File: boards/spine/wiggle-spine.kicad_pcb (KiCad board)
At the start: 2 copper layers, 173 parts, among them CON1 5-24V 5A, CON2 5-24V 16A, CON3 PLR135, CON4 PLT133, CON5 USB-B, CON6 XLR-3 Female, CON7 USB-A, Q1 IRFML8244, Q2 IRFML8244, Q3 IRFML8244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

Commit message: Component clustering around top and bottom I/O ports
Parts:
- added REF**: 1pin, Connect:1pin, F.Cu at (53.3, 170.2)
- added REF**: 1pin, Connect:1pin, F.Cu at (111.8, 170.2)
- added REF**: 1pin, Connect:1pin, F.Cu at (111.8, 45.7)
- added REF**: 1pin, Connect:1pin, F.Cu at (53.3, 45.7)
- moved C74 224.8 mm to (-57.9, 255.4), turned to 270 degrees
- moved C76 220.3 mm to (-54.9, 260.1)
- moved C77 220.2 mm to (-61.0, 260.1)
- moved U13 219.6 mm to (-55.1, 254.9), turned to 0 degrees
- moved U14 218.5 mm to (-57.9, 259.2)
- moved C75 217.7 mm to (-52.3, 256.0), turned to 270 degrees
- moved C32 209.8 mm to (-28.4, 273.9)
- moved C35 209.8 mm to (-34.6, 290.4)
- moved C36 209.8 mm to (-57.7, 266.3)
- moved C41 209.8 mm to (-28.4, 279.0)
- moved R16 209.8 mm to (-22.1, 267.0)
- moved R17 209.8 mm to (-24.6, 267.0)
- moved R18 209.8 mm to (-17.0, 267.0)
- moved R19 209.8 mm to (-19.6, 267.0)
- moved U7 209.8 mm to (-43.4, 274.1)
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
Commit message: Try 2.7" width
Probably too narrow to fit the DCDCs, but it looks nice doesn't it.
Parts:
- moved R15 232.0 mm to (102.5, 106.2), turned to 270 degrees
- moved C35 228.5 mm to (99.9, 105.7), turned to 270 degrees
- moved C39 225.1 mm to (98.0, 109.7), turned to 180 degrees
- moved C34 224.9 mm to (97.4, 106.2), turned to 90 degrees
- moved C38 224.6 mm to (98.0, 112.3), turned to 180 degrees
- moved C31 223.8 mm to (98.0, 118.0), turned to 180 degrees
- moved C33 223.5 mm to (98.0, 120.5), turned to 180 degrees
- moved C41 214.2 mm to (88.5, 99.6), turned to 270 degrees
- moved C40 210.7 mm to (86.0, 99.6), turned to 270 degrees
- moved C32 207.2 mm to (83.4, 99.6), turned to 270 degrees
- moved C44 206.9 mm to (86.6, 128.8), turned to 90 degrees
- moved U7 203.9 mm to (83.6, 114.6), turned to 180 degrees
- moved C46 203.7 mm to (80.9, 99.6), turned to 270 degrees
- moved R18 201.8 mm to (76.5, 88.1), turned to 180 degrees
- moved R19 200.7 mm to (76.5, 90.7), turned to 180 degrees
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
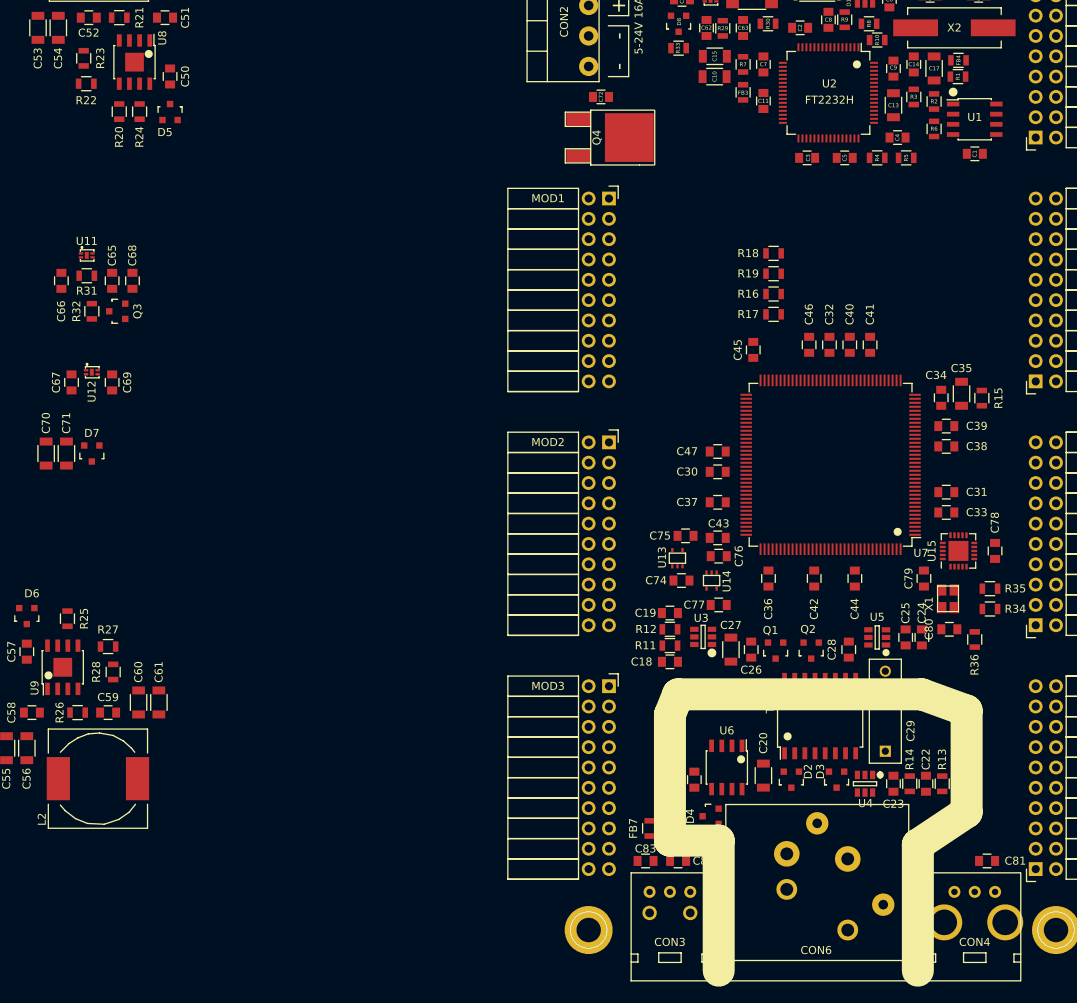
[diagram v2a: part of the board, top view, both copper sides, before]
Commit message: More component packing
If this routing is at all realistic, maybe 2.7" works after all. Haven't placed the DCDCs yet, but I think they'll fit.
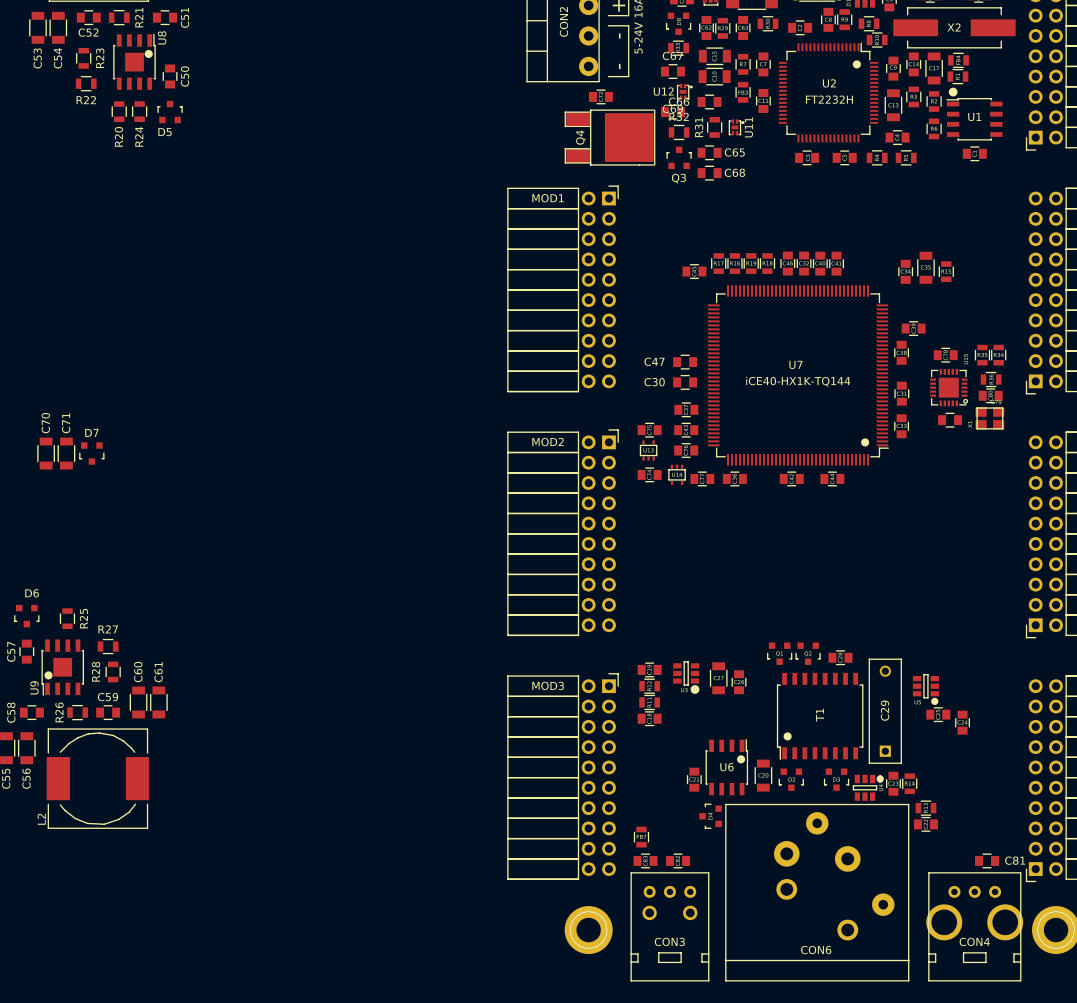
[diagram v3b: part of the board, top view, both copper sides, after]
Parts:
- moved C67 84.6 mm to (63.9, 65.4), turned to 180 degrees
- moved C66 84.1 mm to (68.5, 69.2), turned to 180 degrees
- moved U11 82.6 mm to (71.6, 72.4), turned to 180 degrees
- moved U12 81.8 mm to (65.2, 67.9), turned to 180 degrees
- moved R31 80.6 mm to (69.1, 72.4), turned to 270 degrees
- moved C69 77.8 mm to (63.9, 70.5), turned to 0 degrees
- moved R32 76.7 mm to (64.6, 73.0), turned to 180 degrees
- moved C65 76.4 mm to (68.5, 75.6), turned to 0 degrees
- moved C68 73.4 mm to (68.5, 78.1), turned to 0 degrees
- moved Q3 72.8 mm to (64.6, 76.2), turned to 0 degrees
- moved R36 32.6 mm to (103.6, 103.9), turned to 180 degrees
- moved R34 31.7 mm to (104.6, 100.9), turned to 270 degrees
- moved C80 29.6 mm to (103.6, 105.9), turned to 0 degrees
- moved R35 29.2 mm to (102.6, 100.9), turned to 270 degrees
- moved C78 25.2 mm to (98.0, 100.9), turned to 180 degrees
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
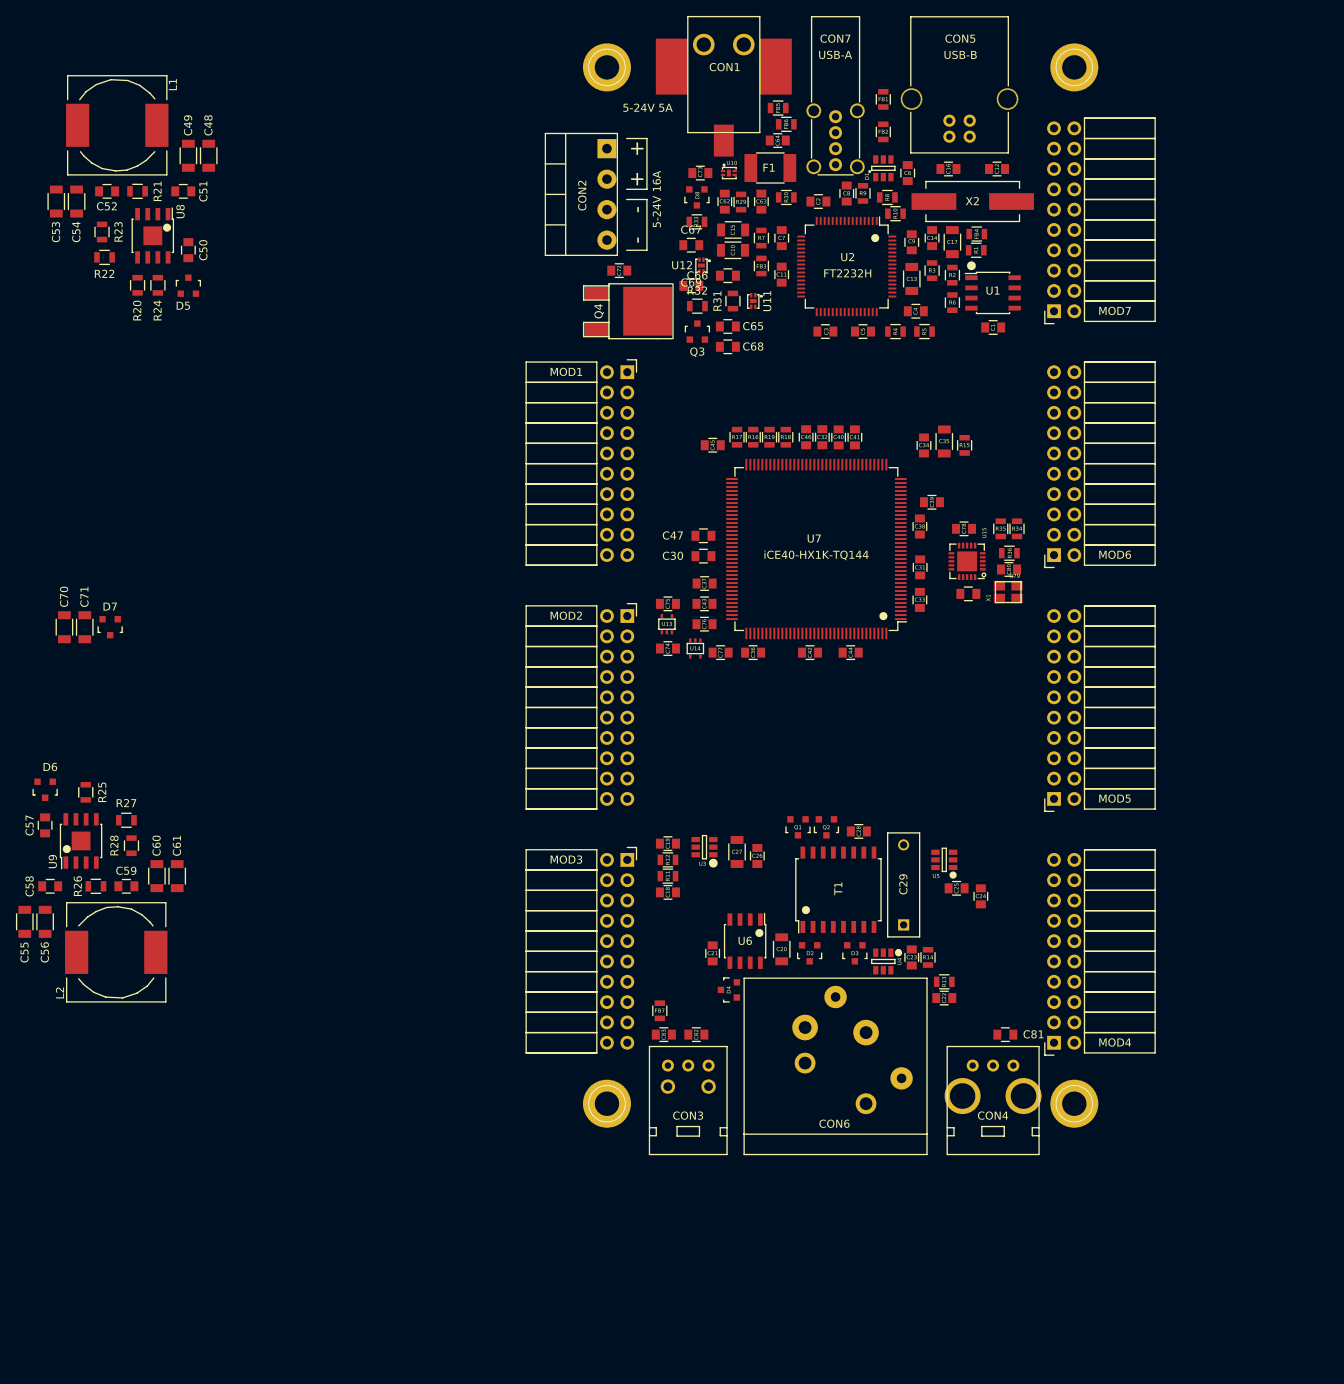
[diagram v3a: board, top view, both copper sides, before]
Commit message: Fix MOD pinouts, and layout for 2.7x5.2in
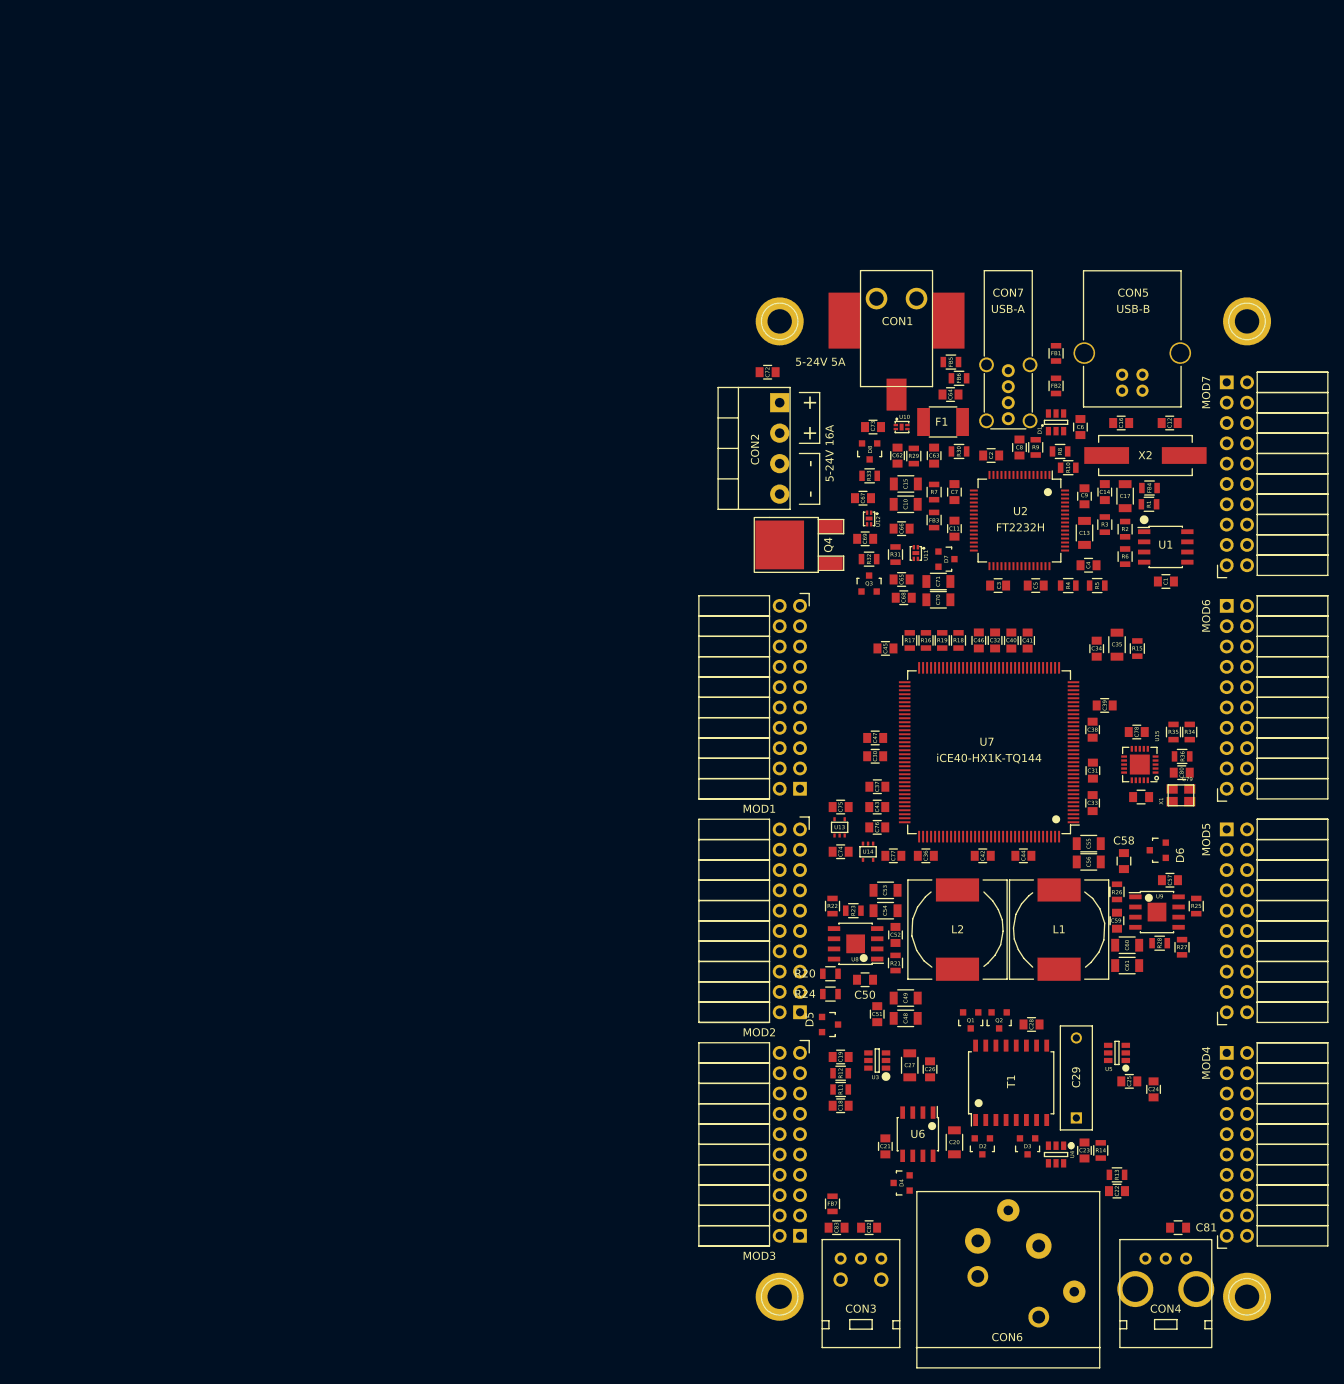
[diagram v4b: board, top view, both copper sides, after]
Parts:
- MOD1, MOD2, MOD3, MOD4, MOD5, MOD6, MOD7: footprint Socket_Strips:Socket_Strip_Angled_2x10 -> Socket_Strips:Socket_Strip_Angled_2x10_Mirror
- moved L1 154.8 mm to (109.9, 151.0), turned to 90 degrees
- moved C57 140.8 mm to (123.7, 144.8), turned to 180 degrees
- moved R25 139.5 mm to (127.0, 148.0)
- moved D6 139.3 mm to (122.2, 141.0), turned to 90 degrees
- moved C48 138.6 mm to (90.7, 162.1), turned to 0 degrees
- moved C49 138.3 mm to (90.7, 159.5), turned to 0 degrees
- moved C52 135.5 mm to (89.4, 151.6), turned to 270 degrees
- moved R21 135.2 mm to (89.4, 155.1), turned to 270 degrees
- moved U9 134.8 mm to (122.1, 148.8), turned to 0 degrees
- moved C53 134.8 mm to (88.2, 146.1), turned to 180 degrees
- moved C51 134.5 mm to (87.1, 161.5), turned to 90 degrees
- moved C54 134.5 mm to (88.2, 148.6), turned to 180 degrees
- moved C58 134.3 mm to (118.0, 142.4), turned to 270 degrees
- moved C55 133.4 mm to (113.6, 140.2), turned to 180 degrees
- moved R27 132.9 mm to (125.2, 153.2), turned to 270 degrees
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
